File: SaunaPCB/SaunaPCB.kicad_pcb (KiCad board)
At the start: 2 copper layers, 199.4 x 109.2 mm, 53 parts, among them J200 KL3RM7.62, J201 KL3RM7.62, J202 KL3RM7.62, J203 KL3RM7.62, J204 KL3RM7.62, J3 KL2RM5.08, J4 KL2RM5.08, J5 KL2RM5.08, J6 KL2RM5.08, K201 Relais_SPDT_CO, K202 Relais_SPDT_CO, K203 Relais_SPDT_CO, K204 Relais_SPDT_CO, K205 Relais_SPDT_CO, K206 Relais_SPDT_CO, K207 Relais_SPDT_CO, U201 LHE05-20B24, U202 4N25, U203 4N25, U204 4N25, U4 ESP32-S3-DevKitC

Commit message: Still working on placement and routing
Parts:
- removed ?: , 
- removed REF** (x4): MountingHole_3.2mm_M3_DIN965, MountingHole:MountingHole_3.2mm_M3_DIN965
- added R211: 10K, Resistor_SMD:R_1206_3216Metric, F.Cu at (180.1, 96.5)
- moved U204 68.3 mm to (242.6, 94.0)
- moved U203 64.5 mm to (221.0, 94.0)
- moved U202 61.1 mm to (199.4, 94.0)
- moved R202 28.4 mm to (139.1, 64.8)
- moved R207 26.9 mm to (154.9, 63.5)
- moved R206 26.9 mm to (141.0, 54.6)
- moved R205 26.9 mm to (141.0, 59.7)
- moved D203 23.5 mm to (160.7, 55.9)
- moved R208 10.2 mm to (236.2, 95.2), turned to -90 degrees
- moved R203 9.65 mm to (214.7, 95.3), turned to -90 degrees
- moved D207 8.28 mm to (242.6, 100.3)
- moved R201 8.13 mm to (232.4, 95.2)
- moved K202 7.62 mm to (233.7, 97.9)
- moved L201 7.62 mm to (232.3, 123.3)
- moved D206 5.85 mm to (221.0, 100.3)
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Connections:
- D205 pad 2: N -> Net-(D205-A)
- D206 pad 2: N -> Net-(D205-A)
- D207 pad 2: N -> Net-(D205-A)
- U202 pad 2: N -> Net-(D205-A)
- U203 pad 2: N -> Net-(D205-A)
- U204 pad 2: N -> Net-(D205-A)
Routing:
- net N: track 78.7 -> 173.3 mm, vias 0 -> 1
- net Relais_2: track 0.00 -> 54.5 mm
- net Net-(D205-A): track 0.00 -> 51.7 mm, vias 0 -> 3
- net +24V: track 65.6 -> 102.8 mm, vias 0 -> 2
- net /Power distribution part/L1_SW: track 80.5 -> 97.5 mm
- net Net-(D205-K): track 0.00 -> 10.7 mm
- net Net-(D207-K): track 0.00 -> 10.7 mm
- net Net-(D206-K): track 0.00 -> 10.6 mm
- net /Power distribution part/L3_SW: track 82.4 -> 91.7 mm
- net /Power distribution part/L2_SW: track 98.9 -> 108.1 mm
- net /Power distribution part/L3_OUT: track 16.5 -> 24.2 mm
- net Net-(R204-Pad1): track 0.00 -> 3.81 mm
- net Net-(R203-Pad1): track 0.00 -> 3.81 mm
- net Net-(R201-Pad2): track 0.00 -> 3.81 mm
- net /Power distribution part/L2_OUT: track 12.9 -> 14.5 mm

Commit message: Still working on placement and routing
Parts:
- added H201: MountingHole, MountingHole:MountingHole_3.2mm_M3_DIN965, F.Cu at (71.1, 47.0)
- added H202: MountingHole, MountingHole:MountingHole_3.2mm_M3_DIN965, F.Cu at (71.1, 143.5)
- added H203: MountingHole, MountingHole:MountingHole_3.2mm_M3_DIN965, F.Cu at (262.9, 47.0)
- added H204: MountingHole, MountingHole:MountingHole_3.2mm_M3_DIN965, F.Cu at (262.9, 143.5)
- added H205: MountingHole, MountingHole:MountingHole_3.2mm_M3_DIN965, F.Cu at (204.5, 143.5)
- D201, D202, D204: footprint Diode_THT:D_DO-41_SOD81_P10.16mm_Horizontal -> Diode_SMD:D_SMA_Handsoldering
- D203: footprint LED_SMD:LED_PLCC-2_3.4x3.0mm_AK -> Connector_JST:JST_EH_B2B-EH-A_1x02_P2.50mm_Vertical
- D205, D206, D207: moved to F.Cu
- R202, R205, R206, R207: footprint Resistor_THT:R_Axial_DIN0207_L6.3mm_D2.5mm_P10.16mm_Horizontal -> Resistor_SMD:R_1206_3216Metric
- R211: footprint Resistor_SMD:R_1206_3216Metric -> Resistor_THT:R_Axial_DIN0207_L6.3mm_D2.5mm_P10.16mm_Horizontal
- moved R207 74.9 mm to (227.3, 82.5), turned to 90 degrees
- moved R211 70.1 mm to (114.3, 120.7)
- moved U4 61.4 mm to (250.2, 44.5), turned to -90 degrees
- moved R206 56.9 mm to (190.5, 82.5), turned to 90 degrees
- moved D202 49.5 mm to (146.1, 80.0)
- moved L203 48.2 mm to (143.5, 124.5)
- moved K206 44.5 mm to (146.1, 97.8)
- moved R204 44.4 mm to (148.6, 95.2)
- moved R210 44.4 mm to (144.8, 95.2)
- moved U202 44.4 mm to (154.9, 94.0)
- moved D205 43.2 mm to (156.2, 100.3)
- moved C204 43.1 mm to (78.8, 47.0)
- moved K201 38.4 mm to (203.2, 97.8)
- moved C205 37.9 mm to (96.6, 47.0)
- moved D201 37.4 mm to (130.8, 80.0)
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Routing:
- net Net-(D205-A): track 51.7 -> 200.6 mm, vias 3 -> 2
- net GND: track 48.8 -> 156.2 mm, vias 0 -> 3
- net +3V3: track 0.00 -> 82.1 mm, vias 0 -> 3
- net /Power distribution part/L2_SW: track 108.1 -> 30.6 mm
- net /Power distribution part/L1_SW: track 97.5 -> 31.8 mm
- net N: track 173.3 -> 109.0 mm, vias 1 -> 0
- net L3: track 20.7 -> 82.7 mm
- net /Power distribution part/L3_SW: track 91.7 -> 31.8 mm
- net Relais_1: track 39.4 -> 95.7 mm, vias 0 -> 3
- net L1_ON: track 141.8 -> 98.0 mm
- net Relais_2: track 54.5 -> 95.2 mm, vias 0 -> 3
- net +24V: track 102.8 -> 136.4 mm, vias 2 -> 0
- net L1: track 49.2 -> 82.5 mm
- net L2: track 19.1 -> 43.9 mm
- net /Power distribution part/L1_OUT: track 16.5 -> 39.2 mm
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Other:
- board size 199.4 x 109.2 mm -> 200 x 110 mm
- board text added: "Light out & main switch"
- board text added: "Line power input"
- board text added: "Power bar N"
- board text added: "Power bar PE"
- board text added: "Sauna oven output"

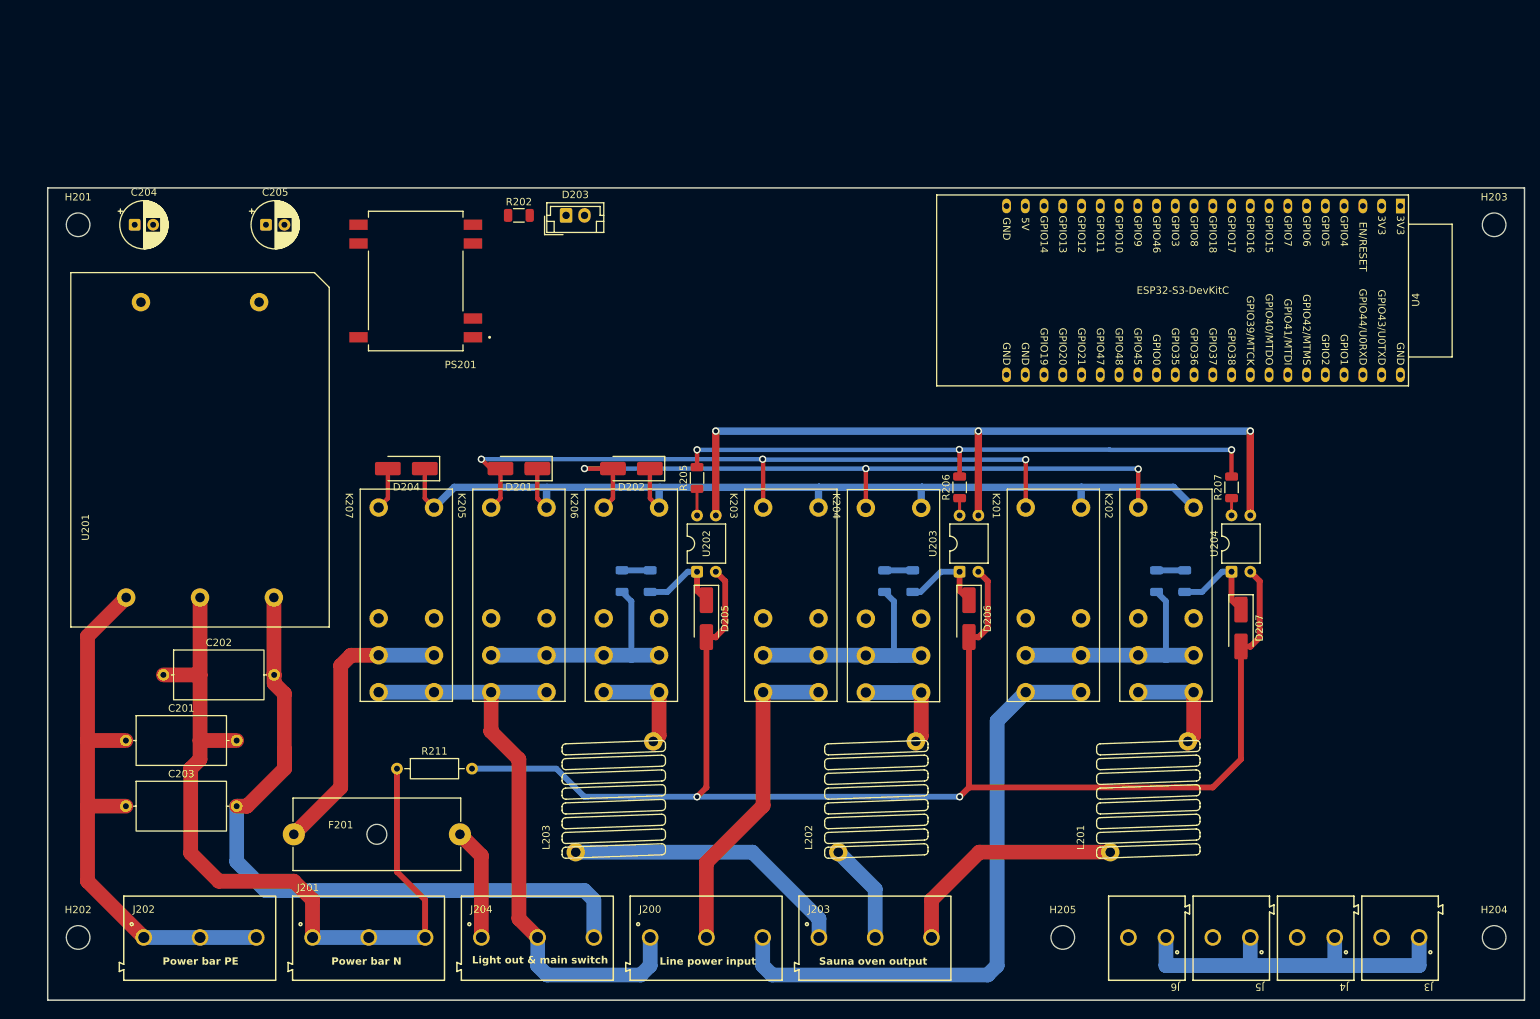
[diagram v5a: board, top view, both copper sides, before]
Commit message: Relay power supply changed
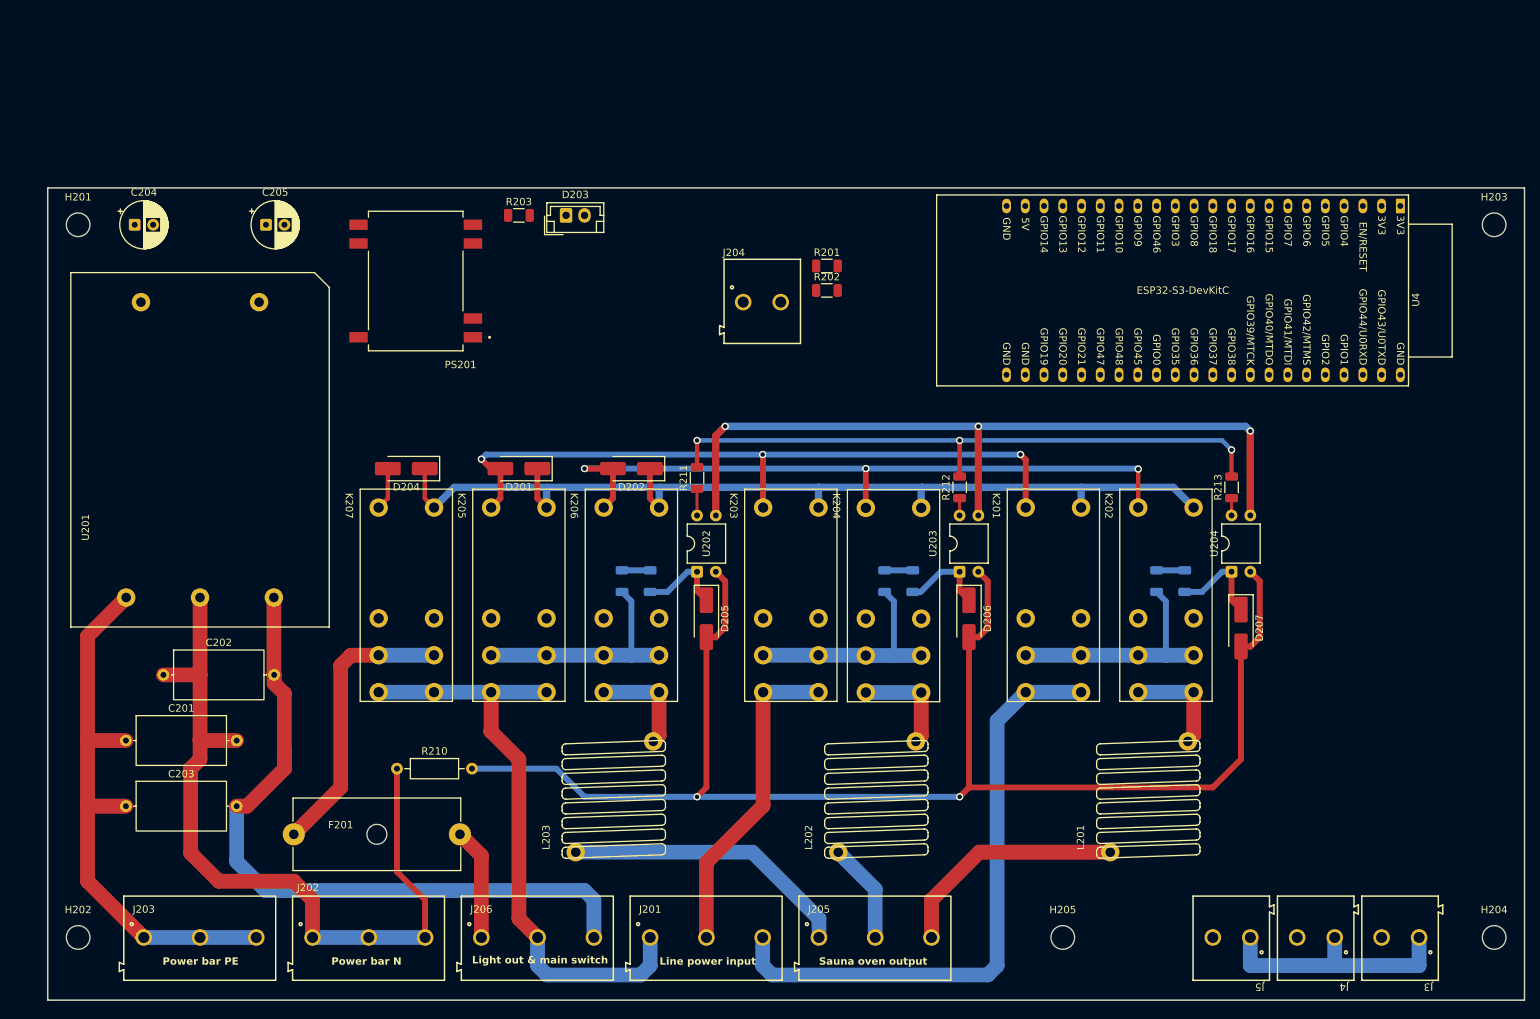
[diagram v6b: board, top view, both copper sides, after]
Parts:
- removed J6: KL2RM5.08, MyConnectors:Terminal_Block_2_RM5.08
- added J204: KL2RM5.08, MyConnectors:Terminal_Block_2_RM5.08, F.Cu at (163.7, 57.5)
- added R201: 100K, Resistor_SMD:R_1206_3216Metric, F.Cu at (172.5, 52.6)
- added R202: 10K, Resistor_SMD:R_1206_3216Metric, F.Cu at (172.5, 55.9)
- renumbered J200 to J201, J201 to J202, J202 to J203, J203 to J205, J204 to J206, R202 to R203, R210 to R204, R209 to R205, R201 to R206, R204 to R207, R203 to R208, R208 to R209, R211 to R210, R205 to R211, R206 to R212, R207 to R213
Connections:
- net Net-(R205-Pad1) renamed L1_SENSE
- D201 pad 1: +24V -> 24VR
- D202 pad 1: +24V -> 24VR
- D204 pad 1: +24V -> 24VR
- K201 pad 11a: /Power distribution part/L1_SW -> /Power distribution part/L3_SW
- K201 pad 11b: /Power distribution part/L1_SW -> /Power distribution part/L3_SW
- K201 pad A1: +24V -> 24VR
- K202 pad 11a: /Power distribution part/L1_SW -> /Power distribution part/L3_SW
- K202 pad 11b: /Power distribution part/L1_SW -> /Power distribution part/L3_SW
- K202 pad A1: +24V -> 24VR
- K203 pad A1: +24V -> 24VR
- K204 pad A1: +24V -> 24VR
- K205 pad 11a: /Power distribution part/L3_SW -> /Power distribution part/L1_SW
- K205 pad 11b: /Power distribution part/L3_SW -> /Power distribution part/L1_SW
- K205 pad A1: +24V -> 24VR
- K206 pad 11a: /Power distribution part/L3_SW -> /Power distribution part/L1_SW
- K206 pad 11b: /Power distribution part/L3_SW -> /Power distribution part/L1_SW
- K206 pad A1: +24V -> 24VR
- K207 pad A1: +24V -> 24VR
- R204 pad 1: /Power distribution part/L3_SW -> /Power distribution part/L1_SW
- R206 pad 1: /Power distribution part/L1_SW -> /Power distribution part/L3_SW
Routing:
- net 24VR: track 0.00 -> 136.4 mm
- net +24V: track 136.4 -> 0.00 mm
- net GND: track 156.2 -> 141.8 mm
- net +3V3: track 82.1 -> 85.0 mm
- net Relais_1: track 95.7 -> 96.9 mm

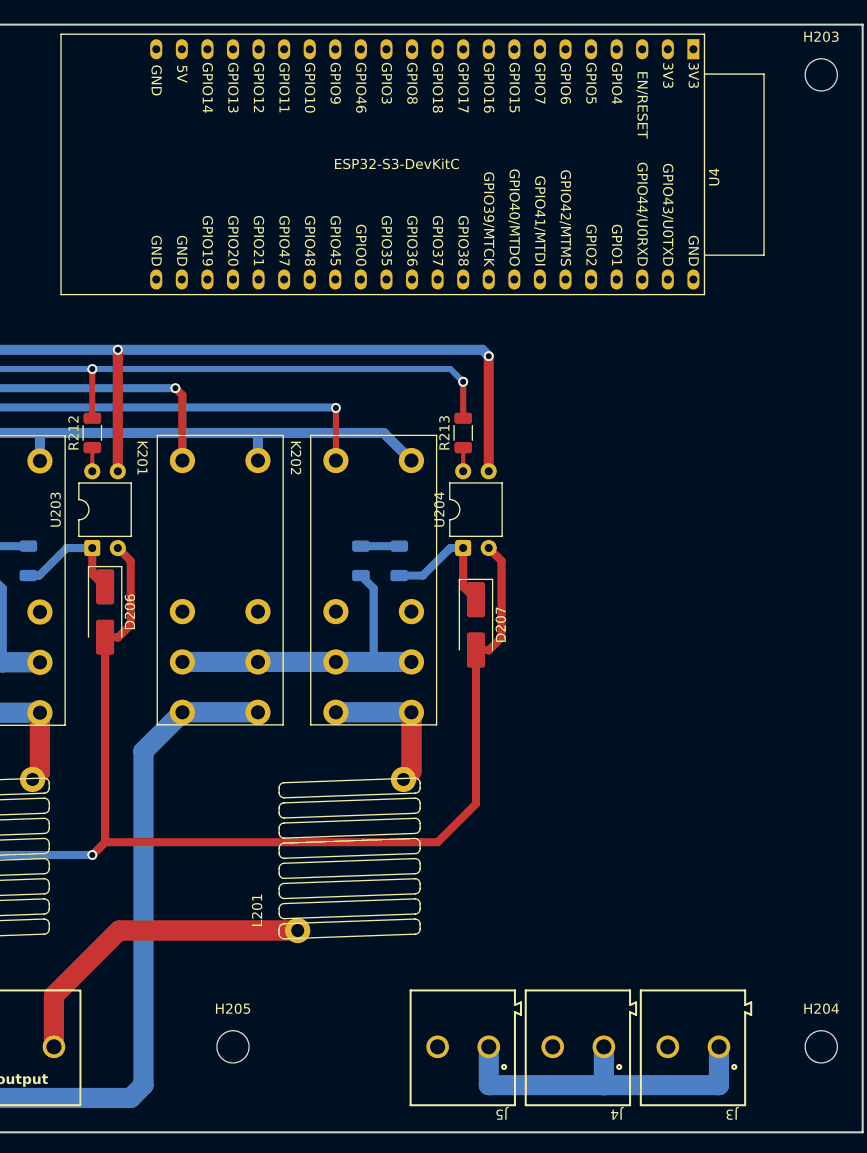
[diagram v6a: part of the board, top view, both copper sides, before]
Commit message: Working on schematic: - Own ESP32 Devkit V4 device used. - ESP32 connections added (all signals from page on connected)
- Next steps: Connection to LCD, Relay driver, Encoder Interface and standby LED
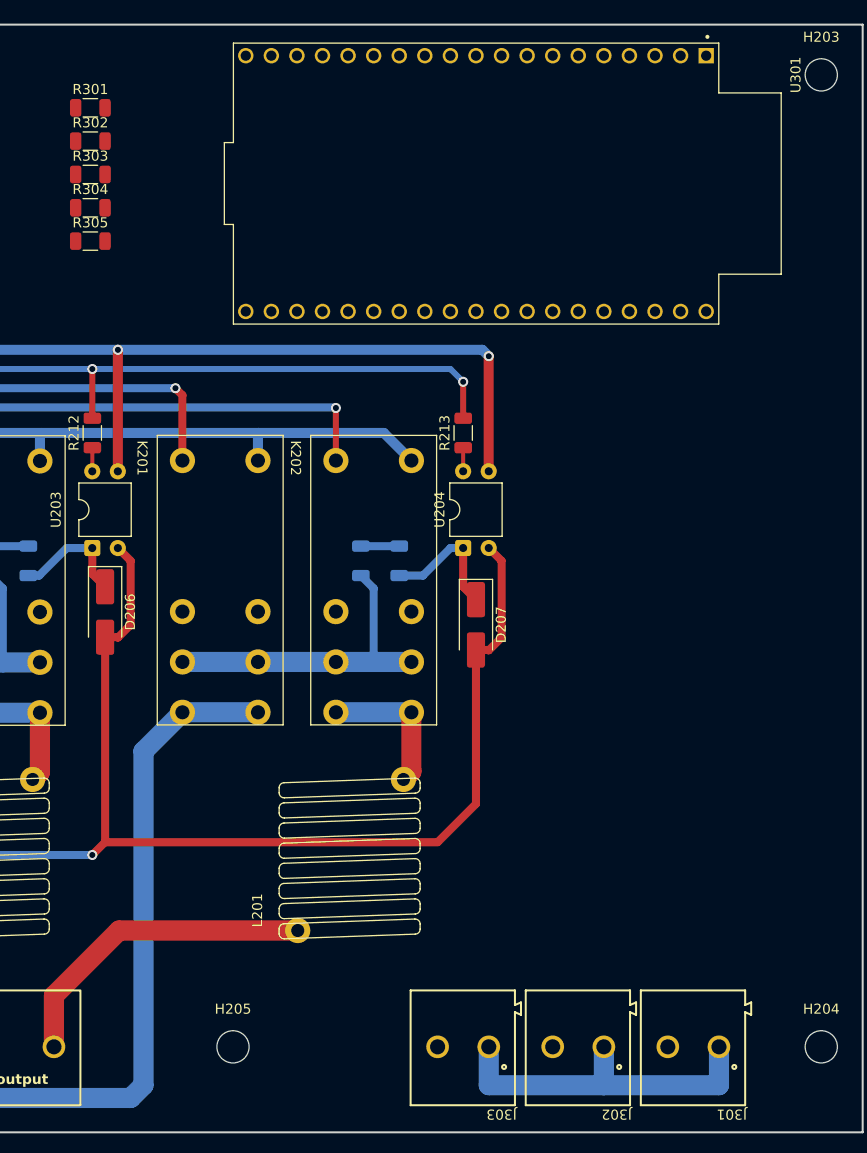
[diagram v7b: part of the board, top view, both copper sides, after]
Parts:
- removed U4: ESP32-S3-DevKitC, Espreessif ESP32:ESP32-S3-DevKitC
- added R301: 10K, Resistor_SMD:R_1206_3216Metric, F.Cu at (190.3, 50.3)
- added R302: 10K, Resistor_SMD:R_1206_3216Metric, F.Cu at (190.3, 53.6)
- added R303: 10K, Resistor_SMD:R_1206_3216Metric, F.Cu at (190.3, 56.9)
- added R304: 2K2, Resistor_SMD:R_1206_3216Metric, F.Cu at (190.3, 60.2)
- added R305: 2K2, Resistor_SMD:R_1206_3216Metric, F.Cu at (190.3, 63.5)
- added U301: ESP32-DEVKITC, MyESP32:ESP32_DevKit_V4, F.Cu at (228.6, 57.8)
- renumbered J3 to J301, J4 to J302, J5 to J303
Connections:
- net L1_SENSE renamed L1_Sense
- net L2_SENSE renamed L2_Sense
- net L3_SENSE renamed L3_Sense
- J301 pad 2: Light_on_off -> Light_OnOff
- J302 pad 2: Standby_On -> Standby_OnOff
